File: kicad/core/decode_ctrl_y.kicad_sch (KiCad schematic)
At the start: 18 parts, among them J40 ADDR_NH0, J41 ADDR_NH1, J42 ADDR_NH2, J43 ADDR_NL0, J44 ADDR_NL1, J45 ADDR_NL2, J52 DEC_EN, J53 BANK_EN, J54 REV_EN_n

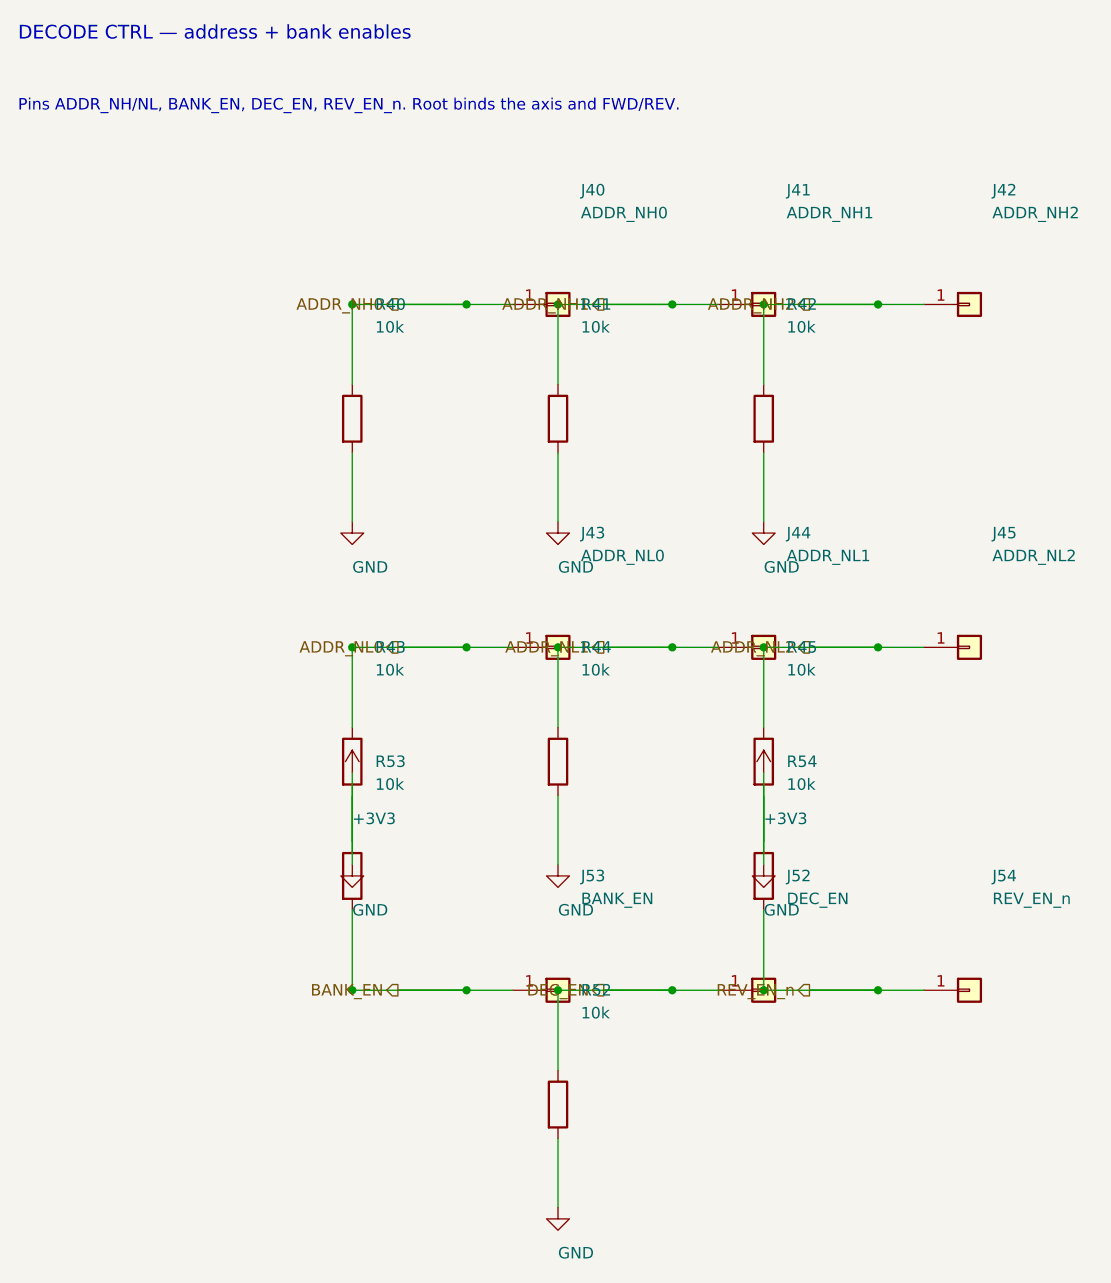
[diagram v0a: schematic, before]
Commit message: Prove the 2×2 access cycle from the address pins through decode, drive, and the sense latch.
Three current sinks, the diode matrix, and drive groups 0--7 are on the schematic. The four-core decks are the gate; weave inductance is still an open input.
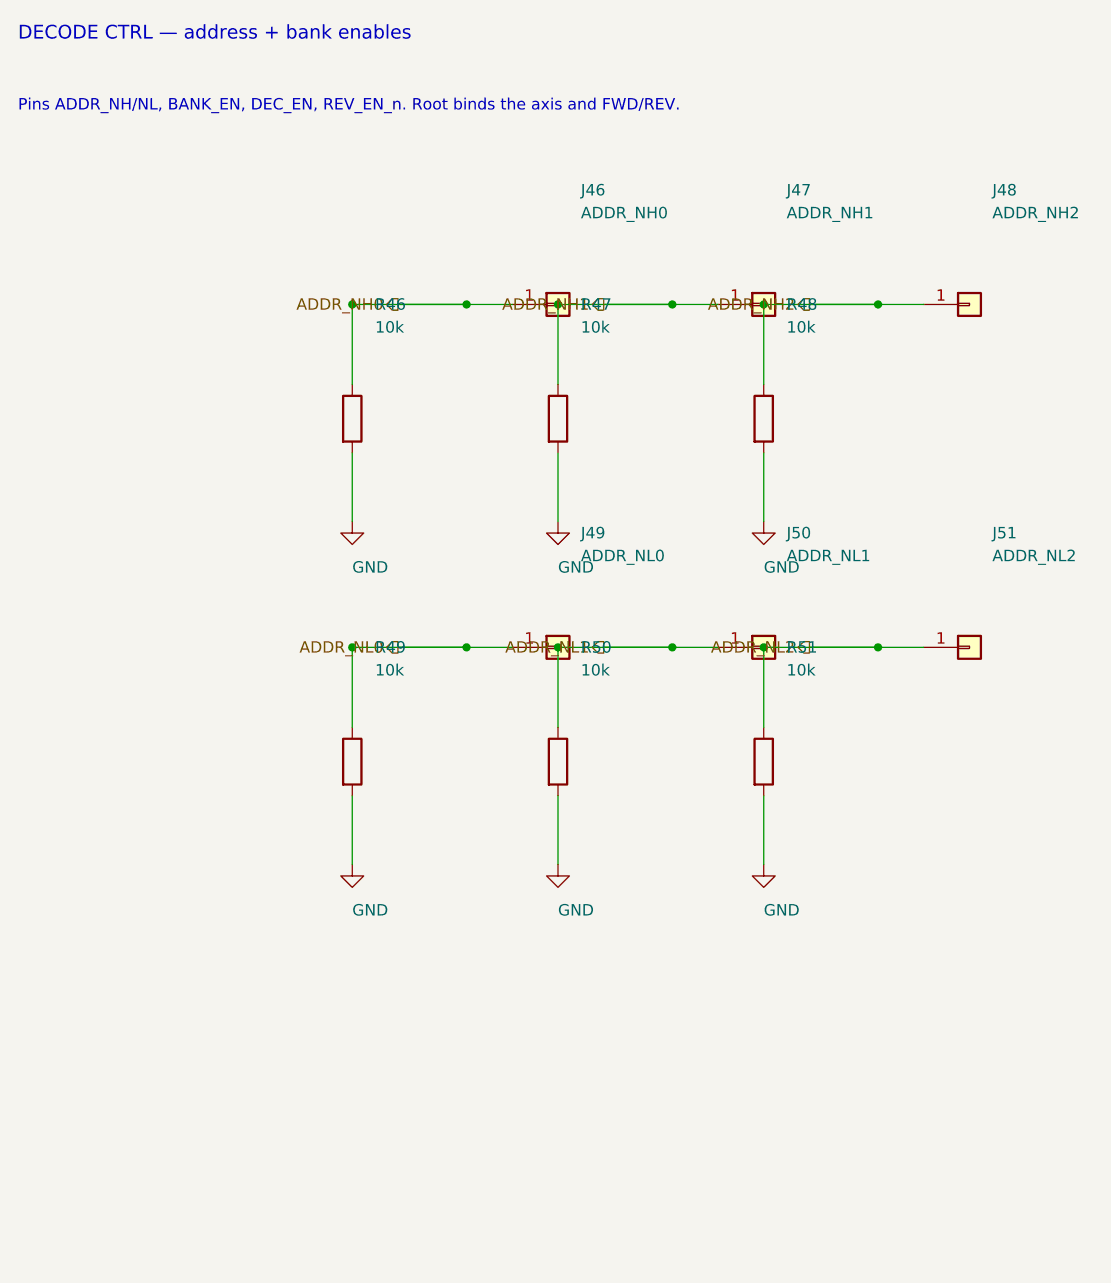
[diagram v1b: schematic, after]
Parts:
- removed J40: ADDR_NH0, Connector_PinHeader_2.54mm:PinHeader_1x01_P2.54mm_Vertical, symbol Connector:Conn_01x01
- removed J41: ADDR_NH1, Connector_PinHeader_2.54mm:PinHeader_1x01_P2.54mm_Vertical, symbol Connector:Conn_01x01
- removed J42: ADDR_NH2, Connector_PinHeader_2.54mm:PinHeader_1x01_P2.54mm_Vertical, symbol Connector:Conn_01x01
- removed J43: ADDR_NL0, Connector_PinHeader_2.54mm:PinHeader_1x01_P2.54mm_Vertical, symbol Connector:Conn_01x01
- removed J44: ADDR_NL1, Connector_PinHeader_2.54mm:PinHeader_1x01_P2.54mm_Vertical, symbol Connector:Conn_01x01
- removed J45: ADDR_NL2, Connector_PinHeader_2.54mm:PinHeader_1x01_P2.54mm_Vertical, symbol Connector:Conn_01x01
- removed J52: DEC_EN, Connector_PinHeader_2.54mm:PinHeader_1x01_P2.54mm_Vertical, symbol Connector:Conn_01x01
- removed J53: BANK_EN, Connector_PinHeader_2.54mm:PinHeader_1x01_P2.54mm_Vertical, symbol Connector:Conn_01x01
- removed J54: REV_EN_n, Connector_PinHeader_2.54mm:PinHeader_1x01_P2.54mm_Vertical, symbol Connector:Conn_01x01
- removed R40, R41, R42, R43, R44, R45, R52, R53, R54: 10k, Resistor_SMD:R_0805_2012Metric, symbol Device:R
- added J46: ADDR_NH0, Connector_PinHeader_2.54mm:PinHeader_1x01_P2.54mm_Vertical, symbol Connector:Conn_01x01
- added J47: ADDR_NH1, Connector_PinHeader_2.54mm:PinHeader_1x01_P2.54mm_Vertical, symbol Connector:Conn_01x01
- added J48: ADDR_NH2, Connector_PinHeader_2.54mm:PinHeader_1x01_P2.54mm_Vertical, symbol Connector:Conn_01x01
- added J49: ADDR_NL0, Connector_PinHeader_2.54mm:PinHeader_1x01_P2.54mm_Vertical, symbol Connector:Conn_01x01
- added J50: ADDR_NL1, Connector_PinHeader_2.54mm:PinHeader_1x01_P2.54mm_Vertical, symbol Connector:Conn_01x01
- added J51: ADDR_NL2, Connector_PinHeader_2.54mm:PinHeader_1x01_P2.54mm_Vertical, symbol Connector:Conn_01x01
- added R46, R47, R48, R49, R50, R51: 10k, Resistor_SMD:R_0805_2012Metric, symbol Device:R
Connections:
- net ADDR_NH0: now also J46.1 (Pin_1), R46.1
- net ADDR_NH1: now also J47.1 (Pin_1), R47.1
- net ADDR_NH2: now also J48.1 (Pin_1), R48.1
- net ADDR_NL0: now also J49.1 (Pin_1), R49.1
- net ADDR_NL1: now also J50.1 (Pin_1), R50.1
- net ADDR_NL2: now also J51.1 (Pin_1), R51.1
- new net GND: R46.2, R47.2, R48.2, R49.2, R50.2, R51.2
